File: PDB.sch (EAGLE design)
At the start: 64 parts, among them IC1 LM555N

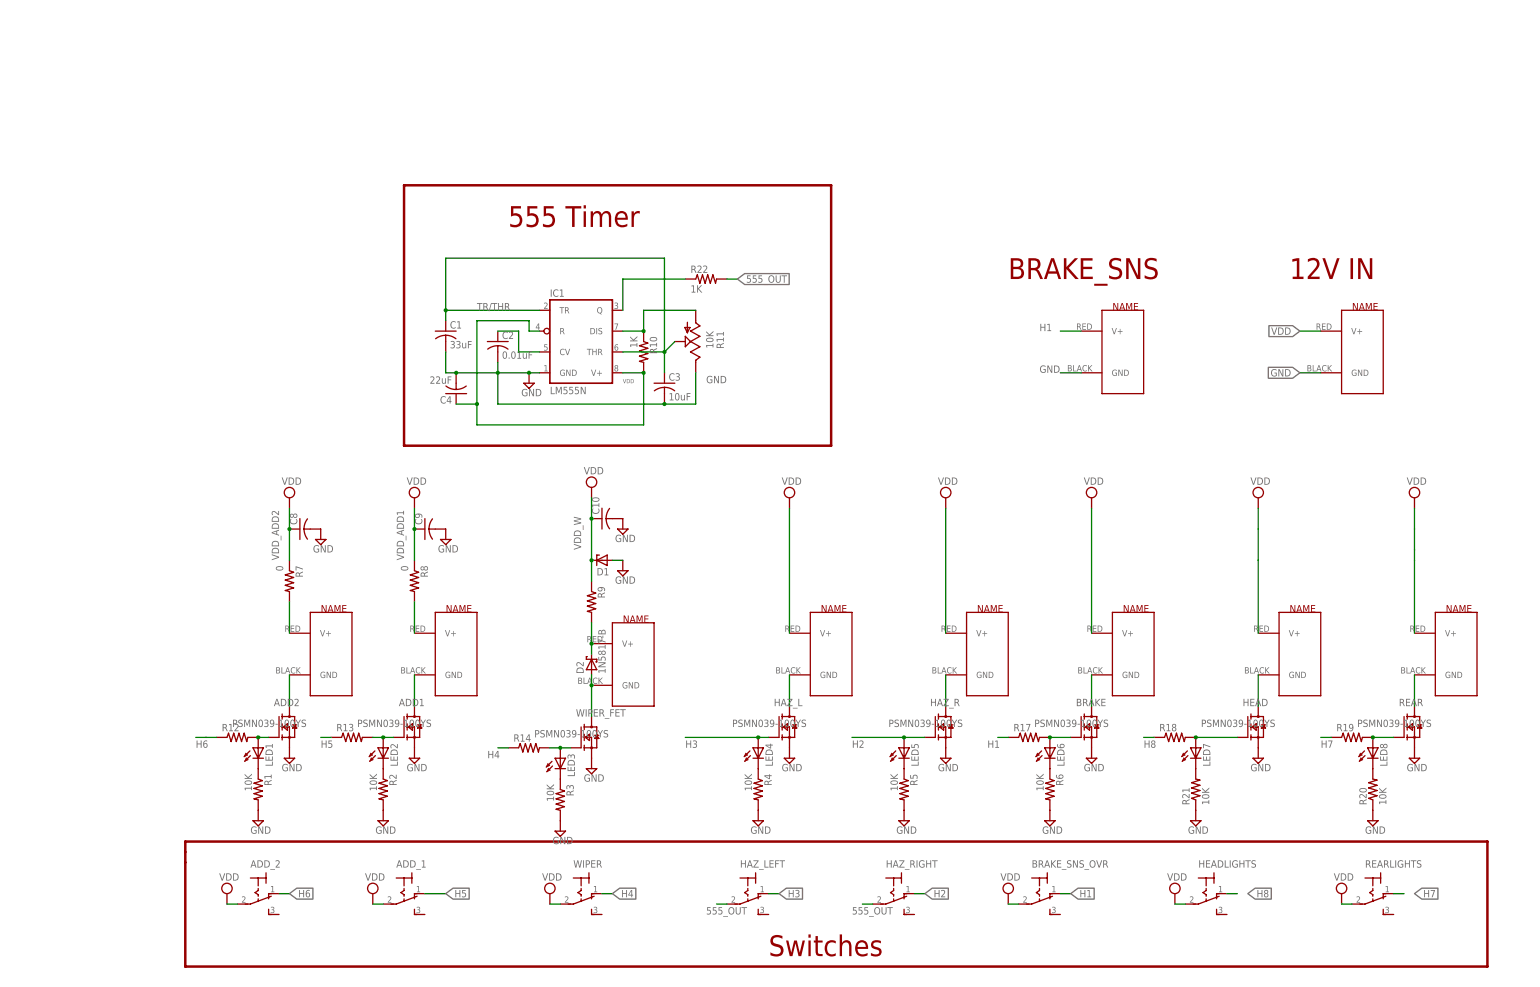
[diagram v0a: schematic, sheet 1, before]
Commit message: wide traces
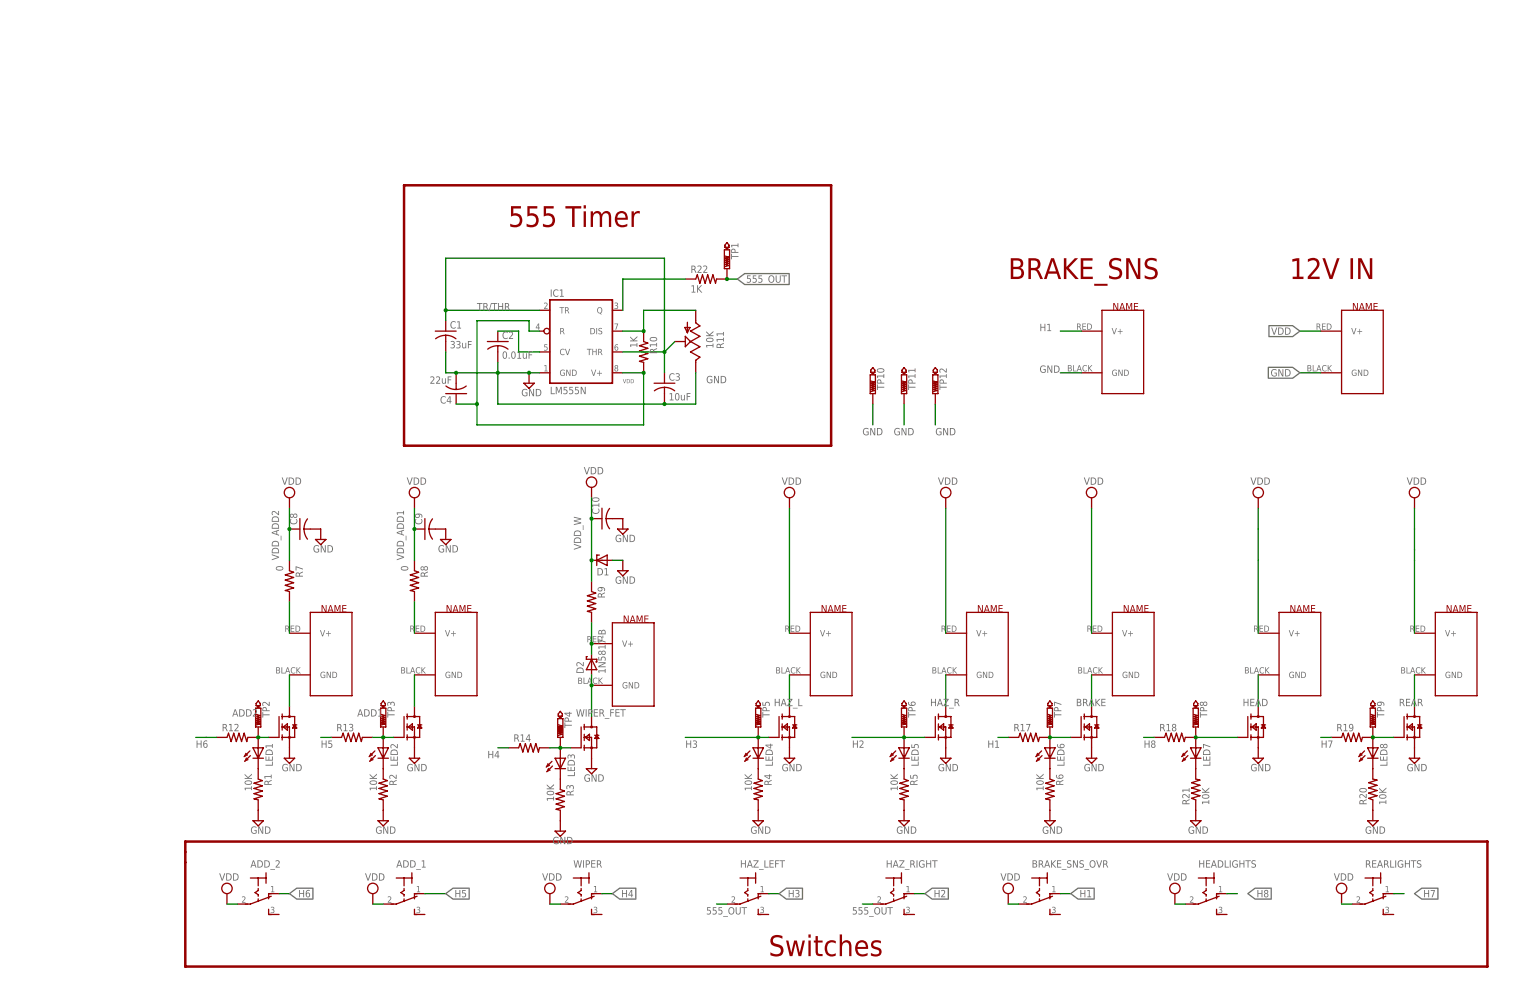
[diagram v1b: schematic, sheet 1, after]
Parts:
- added TP1, TP2, TP3, TP4, TP5, TP6, TP7, TP8, TP9: PTR1B2,54, testpad:PTR1B2,54
- added TP10, TP11, TP12: PTR1PAD1-13Y, testpad:PTR1PAD1-13Y
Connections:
- net 555_OUT: now also TP1.TP
- net GND: now also TP10.TP, TP11.TP, TP12.TP
- net H2: now also TP6.TP
- net H3: now also TP5.TP
- net N$13: now also TP7.TP
- net N$14: now also TP8.TP
- net N$15: now also TP9.TP
- net N$22: now also TP4.TP
- net N$26: now also TP3.TP
- net N$7: now also TP2.TP
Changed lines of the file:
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@@
 <?xml version="1.0" encoding="utf-8"?>
 <!DOCTYPE eagle SYSTEM "eagle.dtd">
-<eagle version="9.2.0">
+<eagle version="9.1.3">
 <drawing>
 <settings>
@@
 <part name="IC1" library="linear" library_urn="urn:adsk.eagle:library:262" deviceset="*555" device="N" package3d_urn="urn:adsk.eagle:package:16409/2" technology="LM"/>
 <part name="C4" library="rcl" library_urn="urn:adsk.eagle:library:334" deviceset="C-US" device="C0805" package3d_urn="urn:adsk.eagle:package:23617/2" value="22uF"/>
+<part name="TP1" library="testpad" library_urn="urn:adsk.eagle:library:385" deviceset="PTR1" device="B2,54" package3d_urn="urn:adsk.eagle:package:27948/1"/>
+<part name="TP2" library="testpad" library_urn="urn:adsk.eagle:library:385" deviceset="PTR1" device="B2,54" package3d_urn="urn:adsk.eagle:package:27948/1"/>
+<part name="TP3" library="testpad" library_urn="urn:adsk.eagle:library:385" deviceset="PTR1" device="B2,54" package3d_urn="urn:adsk.eagle:package:27948/1"/>
+<part name="TP4" library="testpad" library_urn="urn:adsk.eagle:library:385" deviceset="PTR1" device="B2,54" package3d_urn="urn:adsk.eagle:package:27948/1"/>
+<part name="TP5" library="testpad" library_urn="urn:adsk.eagle:library:385" deviceset="PTR1" device="B2,54" package3d_urn="urn:adsk.eagle:package:27948/1"/>
+<part name="TP6" library="testpad" library_urn="urn:adsk.eagle:library:385" deviceset="PTR1" device="B2,54" package3d_urn="urn:adsk.eagle:package:27948/1"/>
+<part name="TP7" library="testpad" library_urn="urn:adsk.eagle:library:385" deviceset="PTR1" device="B2,54" package3d_urn="urn:adsk.eagle:package:27948/1"/>
+<part name="TP8" library="testpad" library_urn="urn:adsk.eagle:library:385" deviceset="PTR1" device="B2,54" package3d_urn="urn:adsk.eagle:package:27948/1"/>
+<part name="TP9" library="testpad" library_urn="urn:adsk.eagle:library:385" deviceset="PTR1" device="B2,54" package3d_urn="urn:adsk.eagle:package:27948/1"/>
+<part name="TP10" library="testpad" library_urn="urn:adsk.eagle:library:385" deviceset="PTR1" device="PAD1-13Y" package3d_urn="urn:adsk.eagle:package:27947/1"/>
+<part name="TP11" library="testpad" library_urn="urn:adsk.eagle:library:385" deviceset="PTR1" device="PAD1-13Y" package3d_urn="urn:adsk.eagle:package:27947/1"/>
+<part name="TP12" library="testpad" library_urn="urn:adsk.eagle:library:385" deviceset="PTR1" device="PAD1-13Y" package3d_urn="urn:adsk.eagle:package:27947/1"/>
 </parts>
 <sheets>
@@
 </plain>
 <instances>
-<instance part="ADD2" gate="G$1" x="-60.96" y="7.62">
+<instance part="ADD2" gate="G$1" x="-60.96" y="7.62" smashed="yes">
 <attribute name="NAME" x="-62.23" y="12.7" size="1.778" layer="95" font="vector"/>
+<attribute name="NAME" x="-72.39" y="10.16" size="1.778" layer="95" font="vector"/>
 </instance>
 <instance part="R7" gate="G$1" x="-58.42" y="43.18" rot="R270">
@@
 <attribute name="VALUE" x="-60.325" y="-3.175" size="1.778" layer="96"/>
 </instance>
-<instance part="ADD1" gate="G$1" x="-30.48" y="7.62">
+<instance part="ADD1" gate="G$1" x="-30.48" y="7.62" smashed="yes">
 <attribute name="NAME" x="-31.75" y="12.7" size="1.778" layer="95" font="vector"/>
+<attribute name="NAME" x="-41.91" y="10.16" size="1.778" layer="95" font="vector"/>
 </instance>
 <instance part="R8" gate="G$1" x="-27.94" y="43.18" rot="R270">
@@
 <attribute name="VALUE" x="-29.845" y="-3.175" size="1.778" layer="96"/>
 </instance>
-<instance part="WIPER_FET" gate="G$1" x="12.7" y="5.08">
+<instance part="WIPER_FET" gate="G$1" x="12.7" y="5.08" smashed="yes">
 <attribute name="NAME" x="11.43" y="10.16" size="1.778" layer="95" font="vector"/>
 </instance>
@@
 <attribute name="VALUE" x="13.335" y="-5.715" size="1.778" layer="96"/>
 </instance>
-<instance part="HAZ_L" gate="G$1" x="60.96" y="7.62">
+<instance part="HAZ_L" gate="G$1" x="60.96" y="7.62" smashed="yes">
 <attribute name="NAME" x="59.69" y="12.7" size="1.778" layer="95" font="vector"/>
 </instance>
@@
 <attribute name="VALUE" x="61.595" y="-3.175" size="1.778" layer="96"/>
 </instance>
-<instance part="HAZ_R" gate="G$1" x="99.06" y="7.62">
+<instance part="HAZ_R" gate="G$1" x="99.06" y="7.62" smashed="yes">
 <attribute name="NAME" x="97.79" y="12.7" size="1.778" layer="95" font="vector"/>
 </instance>
@@
 <attribute name="VALUE" x="99.695" y="-3.175" size="1.778" layer="96"/>
 </instance>
-<instance part="BRAKE" gate="G$1" x="134.62" y="7.62">
+<instance part="BRAKE" gate="G$1" x="134.62" y="7.62" smashed="yes">
 <attribute name="NAME" x="133.35" y="12.7" size="1.778" layer="95" font="vector"/>
 </instance>
@@
 <attribute name="VALUE" x="135.255" y="-3.175" size="1.778" layer="96"/>
 </instance>
-<instance part="HEAD" gate="G$1" x="175.26" y="7.62">
+<instance part="HEAD" gate="G$1" x="175.26" y="7.62" smashed="yes">
 <attribute name="NAME" x="173.99" y="12.7" size="1.778" layer="95" font="vector"/>
 </instance>
@@
 <attribute name="VALUE" x="175.895" y="-3.175" size="1.778" layer="96"/>
 </instance>
-<instance part="REAR" gate="G$1" x="213.36" y="7.62">
+<instance part="REAR" gate="G$1" x="213.36" y="7.62" smashed="yes">
 <attribute name="NAME" x="212.09" y="12.7" size="1.778" layer="95" font="vector"/>
 </instance>
@@
 <attribute name="VALUE" x="-18.796" y="93.091" size="1.778" layer="96" rot="R180"/>
 </instance>
+<instance part="TP1" gate="G$1" x="48.26" y="119.38" rot="R180"/>
+<instance part="TP2" gate="G$1" x="-66.04" y="7.62" rot="R180"/>
+<instance part="TP3" gate="G$1" x="-35.56" y="7.62" rot="R180"/>
+<instance part="TP4" gate="G$1" x="7.62" y="5.08" rot="R180"/>
+<instance part="TP5" gate="G$1" x="55.88" y="7.62" rot="R180"/>
+<instance part="TP6" gate="G$1" x="91.44" y="7.62" rot="R180"/>
+<instance part="TP7" gate="G$1" x="127" y="7.62" rot="R180"/>
+<instance part="TP8" gate="G$1" x="162.56" y="7.62" rot="R180"/>
+<instance part="TP9" gate="G$1" x="205.74" y="7.62" rot="R180"/>
+<instance part="TP10" gate="G$1" x="83.82" y="88.9" rot="R180"/>
+<instance part="TP11" gate="G$1" x="91.44" y="88.9" rot="R180"/>
+<instance part="TP12" gate="G$1" x="99.06" y="88.9" rot="R180"/>
 </instances>
 <busses>
@@
 <wire x1="40.64" y1="86.36" x2="33.02" y2="86.36" width="0.1524" layer="91"/>
 <junction x="33.02" y="86.36"/>
+</segment>
+<segment>
+<pinref part="TP10" gate="G$1" pin="TP"/>
+<wire x1="83.82" y1="86.36" x2="83.82" y2="81.28" width="0.1524" layer="91"/>
+<label x="81.28" y="78.74" size="1.778" layer="95"/>
+</segment>
+<segment>
+<pinref part="TP11" gate="G$1" pin="TP"/>
+<wire x1="91.44" y1="86.36" x2="91.44" y2="81.28" width="0.1524" layer="91"/>
+<label x="88.9" y="78.74" size="1.778" layer="95"/>
+</segment>
+<segment>
+<pinref part="TP12" gate="G$1" pin="TP"/>
+<wire x1="99.06" y1="86.36" x2="99.06" y2="81.28" width="0.1524" layer="91"/>
+<label x="99.06" y="78.74" size="1.778" layer="95"/>
 </segment>
 </net>
@@
 <junction x="55.88" y="5.08"/>
 <wire x1="38.1" y1="5.08" x2="55.88" y2="5.08" width="0.1524" layer="91"/>
+<pinref part="TP5" gate="G$1" pin="TP"/>
 </segment>
 </net>
@@
 <wire x1="78.74" y1="5.08" x2="91.44" y2="5.08" width="0.1524" layer="91"/>
 <junction x="91.44" y="5.08"/>
+<pinref part="TP6" gate="G$1" pin="TP"/>
 </segment>
 </net>
@@
 <wire x1="48.26" y1="116.84" x2="50.8" y2="116.84" width="0.1524" layer="91"/>
 <label x="50.8" y="116.84" size="1.778" layer="95" xref="yes"/>
+<pinref part="TP1" gate="G$1" pin="TP"/>
+<junction x="48.26" y="116.84"/>
 </segment>
 </net>
@@
 <wire x1="132.08" y1="5.08" x2="127" y2="5.08" width="0.1524" layer="91"/>
 <junction x="127" y="5.08"/>
+<pinref part="TP7" gate="G$1" pin="TP"/>
 </segment>
 </net>
@@
 <wire x1="172.72" y1="5.08" x2="162.56" y2="5.08" width="0.1524" layer="91"/>
 <junction x="162.56" y="5.08"/>
+<pinref part="TP8" gate="G$1" pin="TP"/>
 </segment>
 </net>
@@
 <wire x1="210.82" y1="5.08" x2="205.74" y2="5.08" width="0.1524" layer="91"/>
 <junction x="205.74" y="5.08"/>
+<pinref part="TP9" gate="G$1" pin="TP"/>
 </segment>
 </net>
@@
 <wire x1="7.62" y1="2.54" x2="5.08" y2="2.54" width="0.1524" layer="91"/>
 <junction x="7.62" y="2.54"/>
+<pinref part="TP4" gate="G$1" pin="TP"/>
 </segment>
 </net>
@@
 <wire x1="-35.56" y1="5.08" x2="-38.1" y2="5.08" width="0.1524" layer="91"/>
 <junction x="-35.56" y="5.08"/>
+<pinref part="TP3" gate="G$1" pin="TP"/>
 </segment>
 </net>
@@
 <junction x="-66.04" y="5.08"/>
 <pinref part="R12" gate="G$1" pin="2"/>
-</segment>
-</net>
+<pinref part="TP2" gate="G$1" pin="TP"/>
+</segment>
+</net>
